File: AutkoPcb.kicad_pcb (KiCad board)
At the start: 2 copper layers, 83.8 x 113.2 mm, 60 parts, among them IC201 TEENSY_4.1, J101 JST 2.56mm, J102 JST 2.56mm, J103 JST 2.56mm, J104 JST 2.56mm, J105 JST 2.56mm, J106 Conn_01x10_Male, J107 JST 2.56mm, J108 JST 2.56mm, J109 JST 2.56mm, J110 JST 2.56mm, J111 JST 2.56mm, J112 JST 2.56mm, J113 JST 2.56mm, J401 Conn_01x03_Male, J501 Conn_01x03_Male, J601 JST 2.56mm, J701 JST 2.56mm, J801 JST 2.56mm, J901 ARK 5mm, J902 Barrel_Jack_MountingPin, J903 Barrel_Jack_MountingPin, J904 ARK 5mm, J905 JST 2.54mm, J906 JST 2.54mm, J907 JST 2.56mm, SW1001 SW_Push, SW1101 SW_Push, SW1201 SW_Push, SW1301 SW_Push, U901 AZ1117-3.3

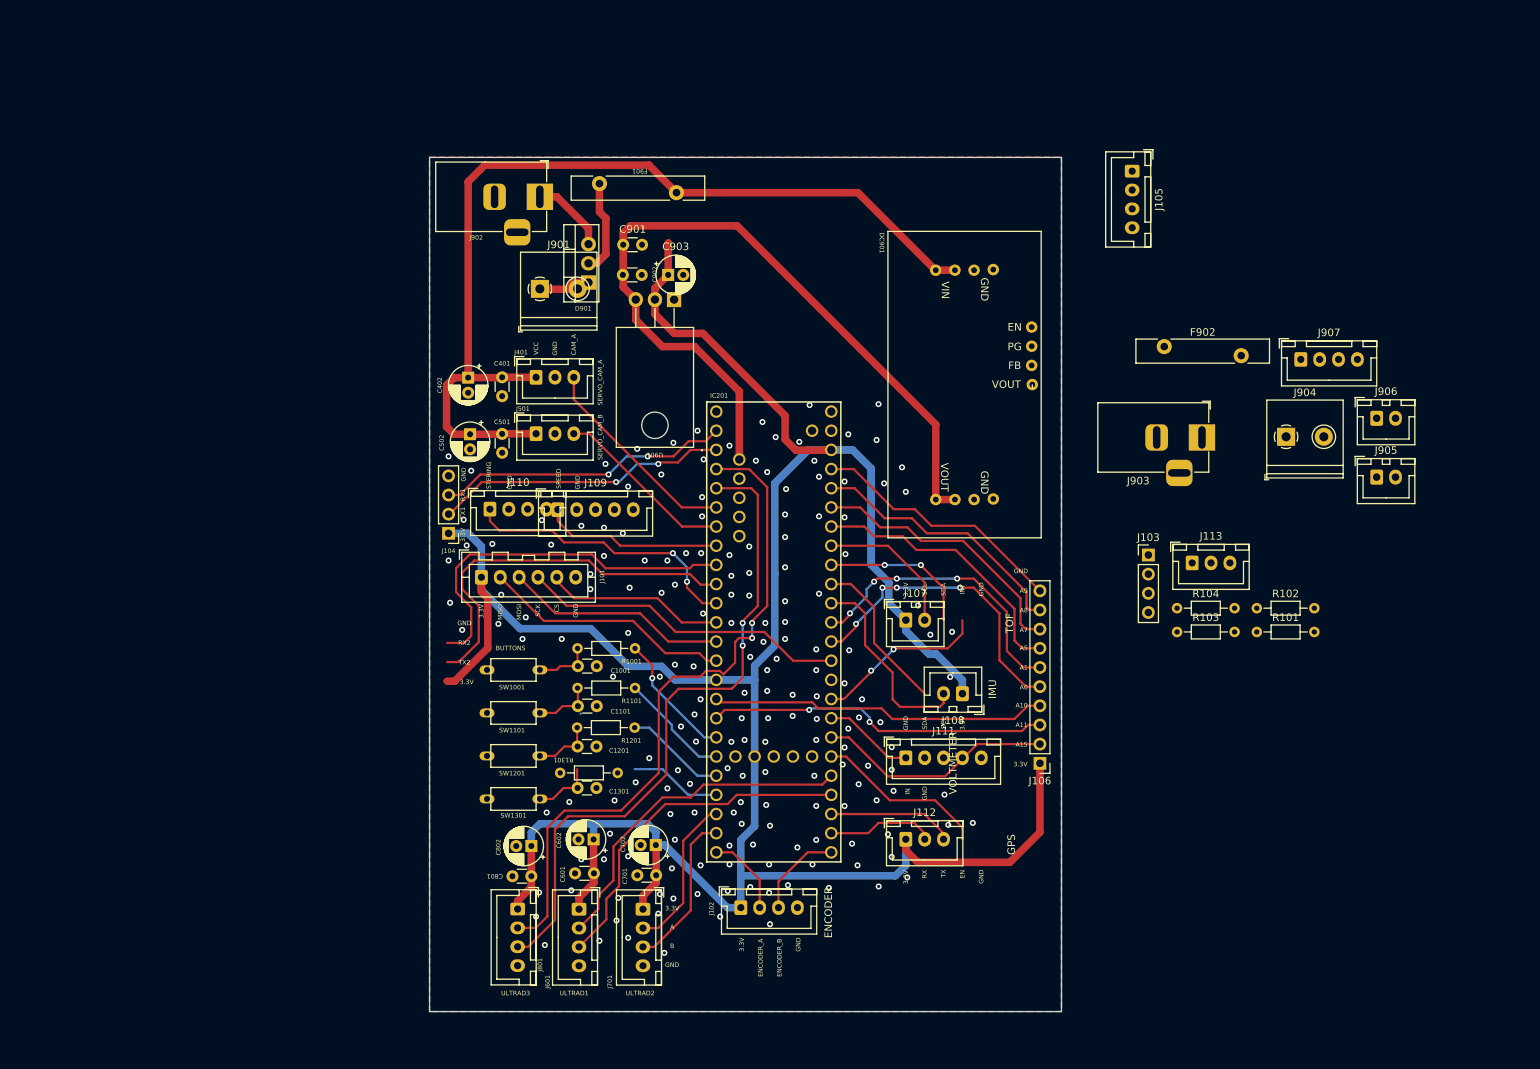
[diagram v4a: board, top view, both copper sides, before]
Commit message: layout update moved power section to the bottom of the board, ibom generated, changed footprint for switches
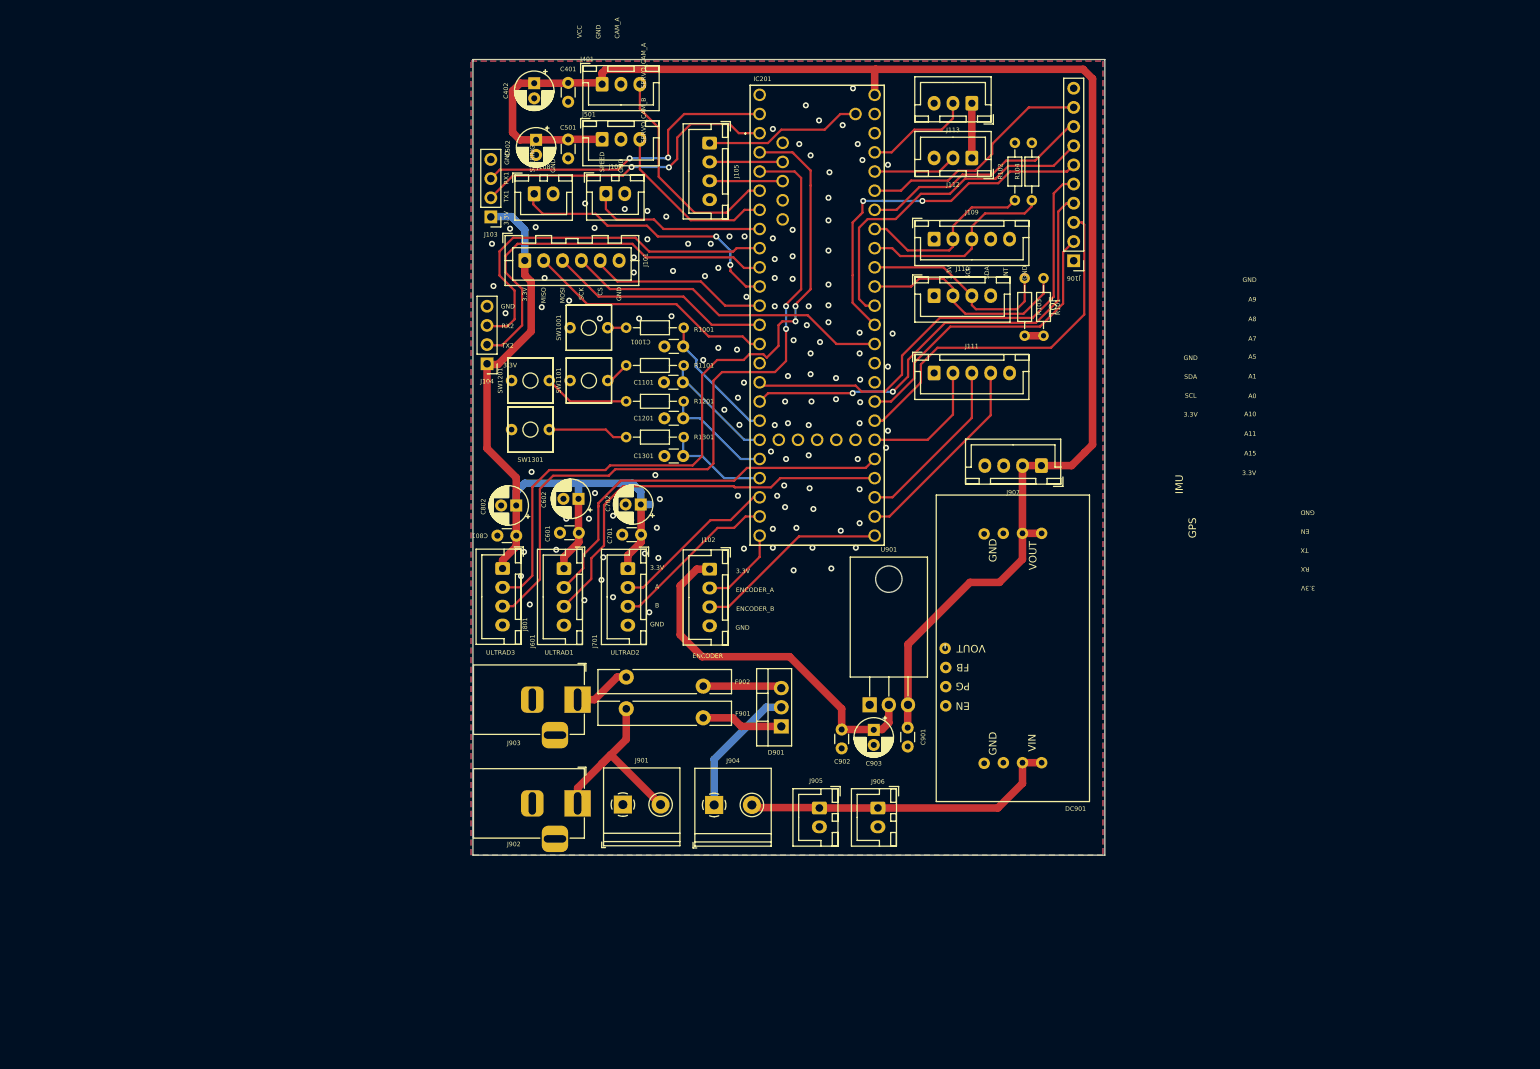
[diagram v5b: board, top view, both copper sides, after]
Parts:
- SW1001, SW1101, SW1201, SW1301: footprint Tact Switch 3x6 mm 5 mm THT:DIP-2_236_ELL -> Tact Switch 6x6 mm 5 mm THT:Tact Switch 6x6mm 5mm
- moved J103 98.0 mm to (107.0, 45.1), turned to 180 degrees
- moved J112 90.7 mm to (170.8, 37.2), turned to 180 degrees
- moved J904 90.2 mm to (136.6, 123.0)
- moved J903 89.8 mm to (118.5, 109.0)
- moved J108 87.2 mm to (112.8, 42.0), turned to 0 degrees
- moved J905 85.9 mm to (150.6, 123.4), turned to -90 degrees
- moved J906 83.9 mm to (158.3, 123.4), turned to -90 degrees
- moved J902 80.5 mm to (118.5, 122.8)
- moved DC901 80.2 mm to (186.3, 122.6), turned to 90 degrees
- moved F902 75.9 mm to (135.2, 107.2), turned to 180 degrees
- moved C901 74.3 mm to (162.2, 112.8), turned to -90 degrees
- moved F901 69.7 mm to (125.0, 110.2)
- moved J901 69.2 mm to (124.5, 123.0)
- moved J107 69.1 mm to (122.2, 42.0)
- moved J113 67.6 mm to (170.8, 30.0), turned to 180 degrees
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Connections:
- net Net-(D901-Pad1) renamed /Power/VIN_DIODE1
- net Net-(D901-Pad3) renamed /Power/VIN_DIODE2
- net Net-(J112-Pad1) renamed /6V_PASSTHROUGHT
- J111 pad 2: /GPS_RX -> /GPS_EN
- J111 pad 4: /GPS_EN -> /GPS_RX
- J904 pad 1: VCC -> /Power/VIN_FUSE
- J904 pad 2: /Power/VIN_FUSE -> VCC
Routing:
- net +3.3V: track 446.1 -> 150.2 mm, vias 6 -> 0
- net GND: track 77.6 -> 0.00 mm, vias 183 -> 122
- net /A11_NC: track 0.00 -> 60.7 mm, vias 0 -> 2
- net /A1_NC: track 0.00 -> 44.8 mm
- net VCC: track 0.00 -> 42.7 mm
- net /TX1_NC: track 0.00 -> 41.9 mm, vias 0 -> 2
- net /RX1_NC: track 0.00 -> 41.3 mm, vias 0 -> 2
- net /A7_NC: track 71.8 -> 31.7 mm
- net /TX2_NC: track 90.2 -> 51.1 mm, vias 2 -> 0
- net /RX2_NC: track 88.6 -> 49.6 mm, vias 2 -> 0
- net /SPEED2: track 0.00 -> 37.7 mm, vias 0 -> 2
- net /IMU_SCL: track 0.00 -> 28.9 mm
- net /A15_NC: track 76.9 -> 48.4 mm, vias 2 -> 0
- net /A16_NC: track 12.1 -> 40.4 mm
- net /GPS_RX: track 0.00 -> 26.5 mm
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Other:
- board size 83.8 x 113.2 mm -> 83.8 x 105.5 mm
- board text removed: "BUTTONS"
- board text removed: "IN"
- board text removed: "VOLTMETER"

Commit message: final board candidate
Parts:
- removed J106: Conn_01x10_Male, Connector_PinHeader_2.54mm:PinHeader_1x10_P2.54mm_Vertical
- added J114: Conn_01x12_Pin, Connector_PinSocket_2.54mm:PinSocket_1x12_P2.54mm_Vertical, F.Cu at (184.3, 56.6)
- moved SW1301 4.36 mm to (114.1, 73.5)
- moved SW1001 3.40 mm to (114.1, 59.8)
- moved SW1101 0.60 mm to (118.1, 66.8)
- moved SW1201 0.25 mm to (110.0, 66.8)
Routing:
- net +3.3V: track 150.2 -> 269.7 mm
- net /TOF_INT: track 0.00 -> 31.2 mm, vias 0 -> 2
- net +5V: track 205.4 -> 198.9 mm
- net /A10_NC: track 63.0 -> 58.8 mm
- net Net-(R1301-Pad2): track 10.6 -> 6.55 mm
- net /A15_NC: track 48.4 -> 44.6 mm
- net /A11_NC: track 60.7 -> 56.9 mm
- net Net-(R1001-Pad2): track 2.44 -> 5.69 mm
- net /A16_NC: track 40.4 -> 37.3 mm
- net /A7_NC: track 31.7 -> 29.7 mm
- net /GPS_EN: track 17.3 -> 15.3 mm
- net /TX2_NC: track 51.1 -> 49.3 mm
- net /RX2_NC: track 49.6 -> 47.9 mm
- net /A1_NC: track 44.8 -> 43.6 mm
- net /A6_NC: track 31.0 -> 29.7 mm
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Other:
- board text added: "5V"
- board text added: "A16"
- board text added: "A6"
- board text added: "D+"
- board text added: "D-"
- board text added: "ON SWITCH"
- board text added: "PASS"
- board text added: "SPEED1"
- board text added: "SPEED2"
- board text added: "STEER1"
- board text added: "STEER2"
- board text added: "STEERING"
- board text added: "USB"
- board text added: "VIN"
- board text added: "VUSB"
- board text removed: "A5"
- board text removed: "A8"
- board text removed: "A9"
- board text removed: "SPEED"
- board text removed: "STERING"
